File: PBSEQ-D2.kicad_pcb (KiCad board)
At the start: 2 copper layers, 19 x 19 mm, 22 parts, among them J1 POWER IN, J2 POWER OUT, J3 BUTTON, Q1 AO3401A, Q2 AO3400A, SW1 BUTTON

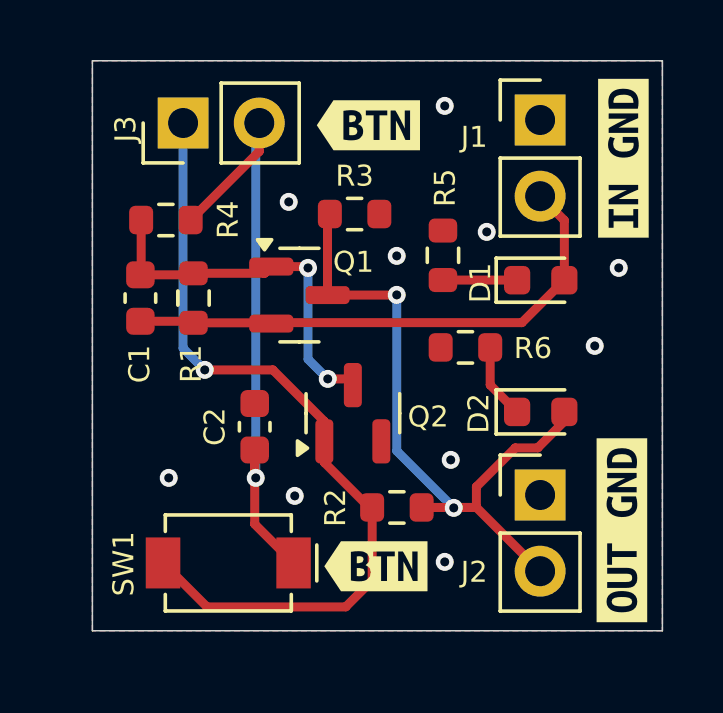
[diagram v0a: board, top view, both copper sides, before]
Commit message: Updated Drill/Place origin
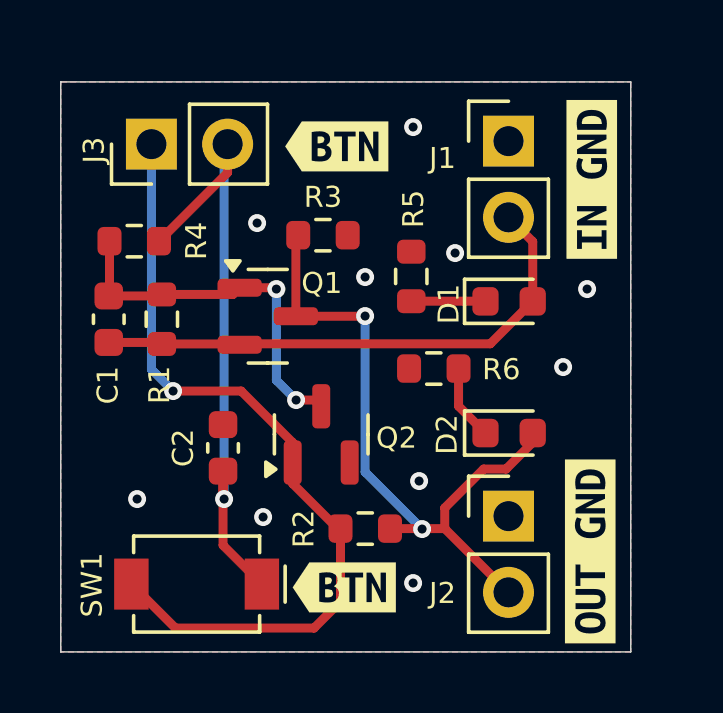
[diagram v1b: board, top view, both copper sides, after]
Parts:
- moved Q1 1.27 mm to (135.9, 99.8)
- moved R6 1.27 mm to (141.4, 101.6)
- moved kibuzzard-663FBC0C 1.27 mm to (138.2, 94.2)
- moved kibuzzard-663FBCF2 1.27 mm to (146.7, 107.7)
- moved C1 1.27 mm to (130.6, 99.9)
- moved C2 1.27 mm to (134.4, 104.2)
- moved D1 1.27 mm to (143.9, 99.3)
- moved D2 1.27 mm to (143.9, 103.7)
- moved G*** 1.27 mm to (138.4, 103.7)
- moved Q2 1.27 mm to (137.7, 103.8)
- moved R1 1.27 mm to (132.4, 99.9)
- moved R2 1.27 mm to (139.2, 106.9)
- moved R4 1.27 mm to (131.4, 97.3)
- moved R5 1.27 mm to (140.7, 98.5)
- moved SW1 1.27 mm to (133.5, 108.7)
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
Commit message: Updated resistor values
* Updated values of `R1` and `R4`. The new values are found to be working with practical testing.
* Updated `Q1` value to `AO3415` based on testing.
* Added net classes and highlights.
* Updated BoM.
* Imported new changes to the PCB.
* No changes in the electrical design.
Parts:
- Q1: value AO3401A -> AO3415
- R4: value 100K -> 470K
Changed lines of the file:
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@@
 				(font
 					(size 1.27 1.27)
+					(thickness 0.15)
 				)
 			)
@@
 				(font
 					(size 1.27 1.27)
+					(thickness 0.15)
 				)
 			)
@@
 				(font
 					(size 1.27 1.27)
+					(thickness 0.15)
 				)
 			)
@@
 				(font
 					(size 1.27 1.27)
+					(thickness 0.15)
 				)
 			)
@@
 				(font
 					(size 1.27 1.27)
+					(thickness 0.15)
 				)
 			)
@@
 				(font
 					(size 1.27 1.27)
+					(thickness 0.15)
 				)
 			)
@@
 				(font
 					(size 1.27 1.27)
+					(thickness 0.15)
 				)
 			)
@@
 				(font
 					(size 1.27 1.27)
+					(thickness 0.15)
 				)
 			)
@@
 				(font
 					(size 1.27 1.27)
+					(thickness 0.15)
 				)
 			)
@@
 				(font
 					(size 1.27 1.27)
+					(thickness 0.15)
 				)
 			)
@@
 				(font
 					(size 1.27 1.27)
+					(thickness 0.15)
 				)
 			)
@@
 				(font
 					(size 1.27 1.27)
+					(thickness 0.15)
 				)
 			)
@@
 				(font
 					(size 1.27 1.27)
+					(thickness 0.15)
 				)
 			)
@@
 				(font
 					(size 1.27 1.27)
+					(thickness 0.15)
 				)
 			)
@@
 				(font
 					(size 1.27 1.27)
+					(thickness 0.15)
 				)
 			)
@@
 			)
 		)
-		(property "Value" "AO3401A"
+		(property "Value" "AO3415"
 			(at 0 1.8 0)
 			(layer "F.Fab")
@@
 				(font
 					(size 1.27 1.27)
+					(thickness 0.15)
 				)
 			)
@@
 				(font
 					(size 1.27 1.27)
+					(thickness 0.15)
 				)
 			)
@@
 				(font
 					(size 1.27 1.27)
+					(thickness 0.15)
 				)
 			)
@@
 			)
 		)
-		(property "MPN" "AO3401A"
+		(property "MPN" "AO3415"
 			(at 0 0 0)
 			(unlocked yes)
@@
 				(font
 					(size 1.27 1.27)
+					(thickness 0.15)
 				)
 			)
@@
 				(font
 					(size 1.27 1.27)
+					(thickness 0.15)
 				)
 			)
@@
 				(font
 					(size 1.27 1.27)
+					(thickness 0.15)
 				)
 			)
@@
 				(font
 					(size 1.27 1.27)
+					(thickness 0.15)
 				)
 			)
@@
 				(font
 					(size 1.27 1.27)
+					(thickness 0.15)
 				)
 			)
@@
 				(font
 					(size 1.27 1.27)
+					(thickness 0.15)
 				)
 			)
@@
 				(font
 					(size 1.27 1.27)
+					(thickness 0.15)
 				)
 			)
@@
 				(font
 					(size 1.27 1.27)
+					(thickness 0.15)
 				)
 			)
@@
 				(font
 					(size 1.27 1.27)
+					(thickness 0.15)
 				)
 			)
@@
 				(font
 					(size 1.27 1.27)
+					(thickness 0.15)
 				)
 			)
@@
 				(font
 					(size 1.27 1.27)
+					(thickness 0.15)
 				)
 			)
@@
 				(font
 					(size 1.27 1.27)
+					(thickness 0.15)
 				)
 			)
@@
 				(font
 					(size 1.27 1.27)
+					(thickness 0.15)
 				)
 			)
@@
 				(font
 					(size 1.27 1.27)
+					(thickness 0.15)
 				)
 			)
@@
 				(font
 					(size 1.27 1.27)
+					(thickness 0.15)
 				)
 			)
@@
 			)
 		)
-		(property "Value" "100K"
+		(property "Value" "470K"
 			(at 0 -0.77 0)
 			(layer "F.Fab")
@@
 				(font
 					(size 1.27 1.27)
+					(thickness 0.15)
 				)
 			)
@@
 				(font
 					(size 1.27 1.27)
+					(thickness 0.15)
 				)
 			)
@@
 				(font
 					(size 1.27 1.27)
+					(thickness 0.15)
 				)
 			)
@@
 			)
 		)
-		(property "MPN" "WR06X1003FTL"
+		(property "MPN" "WR06X4703FTL"
 			(at 0 0 0)
 			(unlocked yes)
@@
 				(font
 					(size 1.27 1.27)
+					(thickness 0.15)
 				)
 			)
@@
 				(font
 					(size 1.27 1.27)
+					(thickness 0.15)
 				)
 			)
@@
 				(font
 					(size 1.27 1.27)
+					(thickness 0.15)
 				)
 			)
@@
 				(font
 					(size 1.27 1.27)
+					(thickness 0.15)
 				)
 			)
@@
 				(font
 					(size 1.27 1.27)
+					(thickness 0.15)
 				)
 			)
@@
 				(font
 					(size 1.27 1.27)
+					(thickness 0.15)
 				)
 			)
@@
 				(font
 					(size 1.27 1.27)
+					(thickness 0.15)
 				)
 			)
@@
 				(font
 					(size 1.27 1.27)
+					(thickness 0.15)
 				)
 			)
@@
 				(font
 					(size 1.27 1.27)
+					(thickness 0.15)
 				)
 			)
@@
 				(font
 					(size 1.27 1.27)
+					(thickness 0.15)
 				)
 			)
@@
 				(font
 					(size 1.27 1.27)
+					(thickness 0.15)
 				)
 			)
@@
 				(font
 					(size 1.27 1.27)
+					(thickness 0.15)
 				)
 			)
@@
 				(font
 					(size 1.27 1.27)
+					(thickness 0.15)
 				)
 			)
@@
 				(font
 					(size 1.27 1.27)
+					(thickness 0.15)
 				)
 			)
@@
 				(font
 					(size 1.27 1.27)
+					(thickness 0.15)
 				)
 			)
@@
 				(font
 					(size 1.27 1.27)
+					(thickness 0.15)
 				)
 			)
@@
 				(font
 					(size 1.27 1.27)
+					(thickness 0.15)
 				)
 			)
@@
 				(font
 					(size 1.27 1.27)
+					(thickness 0.15)
 				)
 			)
@@
 				(font
 					(size 1.27 1.27)
+					(thickness 0.15)
 				)
 			)
@@
 				(font
 					(size 1.27 1.27)
+					(thickness 0.15)
 				)
 			)
@@
 				(font
 					(size 1.27 1.27)
+					(thickness 0.15)
 				)
 			)
@@
 				(font
 					(size 1.27 1.27)
+					(thickness 0.15)
 				)
 			)
@@
 				(font
 					(size 1.27 1.27)
+					(thickness 0.15)
 				)
 			)
@@
 				(font
 					(size 1.27 1.27)
+					(thickness 0.15)
 				)
 			)
@@
 				(font
 					(size 1.27 1.27)
+					(thickness 0.15)
 				)
 				(justify mirror)
@@
 				(font
 					(size 1.27 1.27)
+					(thickness 0.15)
 				)
 				(justify mirror)
@@
 				(font
 					(size 1.27 1.27)
+					(thickness 0.15)
 				)
 				(justify mirror)
@@
 				(font
 					(size 1.27 1.27)
+					(thickness 0.15)
 				)
 				(justify mirror)
@@
 				(font
 					(size 1.27 1.27)
+					(thickness 0.15)
 				)
 				(justify mirror)
@@
 				(font
 					(size 1.27 1.27)
+					(thickness 0.15)
 				)
 				(justify mirror)
